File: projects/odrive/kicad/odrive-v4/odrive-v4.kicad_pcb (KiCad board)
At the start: 2 copper layers, 50 x 30 mm, 0 parts

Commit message: Import the v4 netlist onto a 4-layer board, checkpoint before placement
update_pcb_from_schematic (konnect 0.11.0, live IPC, single undo commit)
lands all 378 footprints with 283 nets and zero conflicts. Getting there
took three tries worth of fixes, all kept: the project fp-lib-table now
registers the 18 standard footprint libraries the sheets reference (the
kicad wrapper's KICAD10_FOOTPRINT_DIR is invisible to project resolution,
same story as the symbol libraries); the seven current shunts move to the
real R_Shunt_Vishay_WSK2512_6332Metric_T2.66mm kelvin footprint (the
T1_T2 name the builder invented does not exist); the OV-latch 74LVC1G74
moves to TSSOP-8 (no DCU footprint in this library snapshot - order the
DCT variant); and the SO3 solder jumpers drop the RoundedPad variant
whose custom-shape pads KiCad 10's typed IPC placement path refuses.
Board outline 120x80mm rounded, In1/In2.Cu added file-based after
learning that adding them with pcbnew open gets clobbered by its next
save. Placement not started - components sit stacked at the import
default.
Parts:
- added C1: 100nF 100V X7R, Capacitor_SMD:C_0603_1608Metric, F.Cu at (6.48, 0.73)
- added C10: 470uF/35V | 220uF/63V, Capacitor_THT:CP_Radial_D10.0mm_P5.00mm, F.Cu at (10.4, 119.4)
- added C100: 2.2uF, Capacitor_SMD:C_0603_1608Metric, F.Cu at (6.48, 1695.1)
- added C101: 2.2uF, Capacitor_SMD:C_0603_1608Metric, F.Cu at (6.48, 1701.6)
- added C11: 470uF/35V | 220uF/63V, Capacitor_THT:CP_Radial_D10.0mm_P5.00mm, F.Cu at (10.4, 134.9)
- added C110: 2.2uF 100V X7R, Capacitor_SMD:C_1210_3225Metric, F.Cu at (7.30, 1787.5)
- added C111: 2.2uF 100V X7R, Capacitor_SMD:C_1210_3225Metric, F.Cu at (7.30, 1795.7)
- added C112: 100nF 100V X7R, Capacitor_SMD:C_0603_1608Metric, F.Cu at (6.48, 1803.0)
- added C113: 100nF 25V, Capacitor_SMD:C_0603_1608Metric, F.Cu at (6.48, 1809.5)
- added C114: 22uF 25V X7R, Capacitor_SMD:C_1210_3225Metric, F.Cu at (7.30, 1816.8)
- added C115: 22uF 25V X7R, Capacitor_SMD:C_1210_3225Metric, F.Cu at (7.30, 1825.0)
- added C116: 10uF 25V X7R, Capacitor_SMD:C_0805_2012Metric, F.Cu at (6.70, 1832.6)
- added C117: 100nF 25V, Capacitor_SMD:C_0603_1608Metric, F.Cu at (6.48, 1839.3)
- added C118: 22uF 25V X7R, Capacitor_SMD:C_1210_3225Metric, F.Cu at (7.30, 1846.7)
- added C119: 22uF 25V X7R, Capacitor_SMD:C_1210_3225Metric, F.Cu at (7.30, 1854.8)
- added C120: 68uF 16V polymer, Capacitor_SMD:CP_Elec_6.3x7.7, F.Cu at (9.70, 1865.0)
- added C122: 1uF 16V, Capacitor_SMD:C_0603_1608Metric, F.Cu at (6.48, 1874.3)
- added C123: 1uF 16V, Capacitor_SMD:C_0603_1608Metric, F.Cu at (6.48, 1880.7)
- added C124: 10uF 16V, Capacitor_SMD:C_0805_2012Metric, F.Cu at (6.70, 1887.5)
- added C125: 1uF 16V, Capacitor_SMD:C_0603_1608Metric, F.Cu at (6.48, 1894.2)
- added C126: 100nF, Capacitor_SMD:C_0603_1608Metric, F.Cu at (6.48, 1900.6)
- added C127: 100nF, Capacitor_SMD:C_0603_1608Metric, F.Cu at (6.48, 1907.1)
- added C128: 100nF, Capacitor_SMD:C_0603_1608Metric, F.Cu at (6.48, 1913.5)
- added C129: 100nF, Capacitor_SMD:C_0603_1608Metric, F.Cu at (6.48, 1920.0)
- added C130: 4.7nF, Capacitor_SMD:C_0603_1608Metric, F.Cu at (6.48, 2122.2)
- added C131: 1uF, Capacitor_SMD:C_0603_1608Metric, F.Cu at (6.48, 2128.7)
- added C132: 100nF, Capacitor_SMD:C_0603_1608Metric, F.Cu at (6.48, -2068.7)
- added C133: 100nF, Capacitor_SMD:C_0603_1608Metric, F.Cu at (6.48, -2062.3)
- added C134: 4.7nF, Capacitor_SMD:C_0603_1608Metric, F.Cu at (6.48, -2055.8)
- added C135: 1uF, Capacitor_SMD:C_0603_1608Metric, F.Cu at (6.48, -2049.3)
- added C136: 10uF, Capacitor_SMD:C_0805_2012Metric, F.Cu at (6.70, -2042.6)
- added C140: 1nF, Capacitor_SMD:C_0603_1608Metric, F.Cu at (6.48, -1934.6)
- added C141: 1nF, Capacitor_SMD:C_0603_1608Metric, F.Cu at (6.48, -1928.1)
- added C142: 1nF, Capacitor_SMD:C_0603_1608Metric, F.Cu at (6.48, -1921.7)
- added C143: 1nF, Capacitor_SMD:C_0603_1608Metric, F.Cu at (6.48, -1915.2)
- added C144: 1nF, Capacitor_SMD:C_0603_1608Metric, F.Cu at (6.48, -1908.7)
- added C145: 1nF, Capacitor_SMD:C_0603_1608Metric, F.Cu at (6.48, -1902.3)
- added C146: 10uF, Capacitor_SMD:C_0805_2012Metric, F.Cu at (6.70, -1895.6)
- added C147: 10uF, Capacitor_SMD:C_0805_2012Metric, F.Cu at (6.70, -1888.6)
- added C148: 1nF, Capacitor_SMD:C_0603_1608Metric, F.Cu at (6.48, -1881.9)
- added C149: 1nF, Capacitor_SMD:C_0603_1608Metric, F.Cu at (6.48, -1875.4)
- added C150: 1nF, Capacitor_SMD:C_0603_1608Metric, F.Cu at (6.48, -1869.0)
- added C151: 1nF, Capacitor_SMD:C_0603_1608Metric, F.Cu at (6.48, -1862.5)
- added C152: 1nF, Capacitor_SMD:C_0603_1608Metric, F.Cu at (6.48, -1856.1)
- added C153: 1uF, Capacitor_SMD:C_0603_1608Metric, F.Cu at (6.48, -1849.6)
- added C154: 1uF, Capacitor_SMD:C_0603_1608Metric, F.Cu at (6.48, -1843.1)
- added C155: 100nF, Capacitor_SMD:C_0603_1608Metric, F.Cu at (6.48, -1836.7)
- added C156: 100nF, Capacitor_SMD:C_0603_1608Metric, F.Cu at (6.48, -1830.2)
- added C157: 100nF, Capacitor_SMD:C_0603_1608Metric, F.Cu at (6.48, -1823.8)
- added C158: 100nF, Capacitor_SMD:C_0603_1608Metric, F.Cu at (6.48, -1817.3)
- added C160: 1uF, Capacitor_SMD:C_0603_1608Metric, F.Cu at (6.48, -1534.5)
- added C161: 100nF, Capacitor_SMD:C_0603_1608Metric, F.Cu at (6.48, -1528.0)
- added C162: 100nF, Capacitor_SMD:C_0603_1608Metric, F.Cu at (6.48, -1521.5)
- added C163: 2.2uF 100V X7R, Capacitor_SMD:C_1210_3225Metric, F.Cu at (7.30, -1514.2)
- added C164: 2.2uF 100V X7R, Capacitor_SMD:C_1210_3225Metric, F.Cu at (7.30, -1506.0)
- added C165: 100nF 100V X7R, Capacitor_SMD:C_0603_1608Metric, F.Cu at (6.48, -1498.7)
- added C166: 1nF, Capacitor_SMD:C_0603_1608Metric, F.Cu at (6.48, -1492.2)
- added C167: 100nF, Capacitor_SMD:C_0603_1608Metric, F.Cu at (6.48, -1485.8)
- added C168: 100nF, Capacitor_SMD:C_0603_1608Metric, F.Cu at (6.48, -1479.3)
- added C169: 100nF, Capacitor_SMD:C_0603_1608Metric, F.Cu at (6.48, -1472.8)
- added C170: 100nF, Capacitor_SMD:C_0603_1608Metric, F.Cu at (6.48, -1466.4)
- added C2: 2.2uF 100V X7R, Capacitor_SMD:C_1210_3225Metric, F.Cu at (7.30, 8.06)
- added C20: 2.2uF 100V X7R, Capacitor_SMD:C_1210_3225Metric, F.Cu at (7.30, 262.2)
- added C21: 2.2uF 100V X7R, Capacitor_SMD:C_1210_3225Metric, F.Cu at (7.30, 270.4)
- added C22: 2.2uF 100V X7R, Capacitor_SMD:C_1210_3225Metric, F.Cu at (7.30, 278.6)
- added C23: 2.2uF 100V X7R, Capacitor_SMD:C_1210_3225Metric, F.Cu at (7.30, 286.8)
- added C24: 2.2uF 100V X7R, Capacitor_SMD:C_1210_3225Metric, F.Cu at (7.30, 295.0)
- added C25: 2.2uF 100V X7R, Capacitor_SMD:C_1210_3225Metric, F.Cu at (7.30, 303.2)
- added C26: 100nF 100V X7R, Capacitor_SMD:C_0603_1608Metric, F.Cu at (6.48, 310.5)
- added C27: 100nF 100V X7R, Capacitor_SMD:C_0603_1608Metric, F.Cu at (6.48, 317.0)
- added C28: 100nF 100V X7R, Capacitor_SMD:C_0603_1608Metric, F.Cu at (6.48, 323.4)
- added C29: 47nF 100V X7R, Capacitor_SMD:C_0805_2012Metric, F.Cu at (6.70, 330.1)
- added C3: 1uF 25V, Capacitor_SMD:C_0603_1608Metric, F.Cu at (6.48, 15.4)
- added C30: 1uF, Capacitor_SMD:C_0603_1608Metric, F.Cu at (6.48, 336.9)
- added C31: 1uF, Capacitor_SMD:C_0603_1608Metric, F.Cu at (6.48, 343.3)
- added C32: 1uF 100V X7R, Capacitor_SMD:C_1210_3225Metric, F.Cu at (7.30, 350.6)
- added C33: 100nF, Capacitor_SMD:C_0603_1608Metric, F.Cu at (6.48, 358.0)
- added C34: 100nF, Capacitor_SMD:C_0603_1608Metric, F.Cu at (6.48, 364.4)
- added C35: 1nF, Capacitor_SMD:C_0603_1608Metric, F.Cu at (6.48, 370.9)
- added C36: 1nF, Capacitor_SMD:C_0603_1608Metric, F.Cu at (6.48, 377.4)
- added C37: 1nF, Capacitor_SMD:C_0603_1608Metric, F.Cu at (6.48, 383.8)
- added C4: 470uF/35V | 220uF/63V, Capacitor_THT:CP_Radial_D10.0mm_P5.00mm, F.Cu at (10.4, 26.4)
- added C40: 2.2uF 100V X7R, Capacitor_SMD:C_1210_3225Metric, F.Cu at (7.30, 719.1)
- added C41: 2.2uF 100V X7R, Capacitor_SMD:C_1210_3225Metric, F.Cu at (7.30, 727.3)
- added C42: 2.2uF 100V X7R, Capacitor_SMD:C_1210_3225Metric, F.Cu at (7.30, 735.5)
- added C43: 2.2uF 100V X7R, Capacitor_SMD:C_1210_3225Metric, F.Cu at (7.30, 743.7)
- added C44: 2.2uF 100V X7R, Capacitor_SMD:C_1210_3225Metric, F.Cu at (7.30, 751.9)
- added C45: 2.2uF 100V X7R, Capacitor_SMD:C_1210_3225Metric, F.Cu at (7.30, 760.1)
- added C46: 100nF 100V X7R, Capacitor_SMD:C_0603_1608Metric, F.Cu at (6.48, 767.5)
- added C47: 100nF 100V X7R, Capacitor_SMD:C_0603_1608Metric, F.Cu at (6.48, 773.9)
- added C48: 100nF 100V X7R, Capacitor_SMD:C_0603_1608Metric, F.Cu at (6.48, 780.4)
- added C49: 47nF 100V X7R, Capacitor_SMD:C_0805_2012Metric, F.Cu at (6.70, 787.1)
- added C5: 470uF/35V | 220uF/63V, Capacitor_THT:CP_Radial_D10.0mm_P5.00mm, F.Cu at (10.4, 41.9)
- added C50: 1uF, Capacitor_SMD:C_0603_1608Metric, F.Cu at (6.48, 793.8)
- added C51: 1uF, Capacitor_SMD:C_0603_1608Metric, F.Cu at (6.48, 800.3)
- added C52: 1uF 100V X7R, Capacitor_SMD:C_1210_3225Metric, F.Cu at (7.30, 807.6)
- added C53: 100nF, Capacitor_SMD:C_0603_1608Metric, F.Cu at (6.48, 814.9)
- added C54: 100nF, Capacitor_SMD:C_0603_1608Metric, F.Cu at (6.48, 821.4)
- added C58: 1nF, Capacitor_SMD:C_0603_1608Metric, F.Cu at (6.48, 827.8)
- added C59: 1nF, Capacitor_SMD:C_0603_1608Metric, F.Cu at (6.48, 834.3)
- added C6: 470uF/35V | 220uF/63V, Capacitor_THT:CP_Radial_D10.0mm_P5.00mm, F.Cu at (10.4, 57.4)
- added C60: 1nF, Capacitor_SMD:C_0603_1608Metric, F.Cu at (6.48, 840.8)
- added C61: 100nF, Capacitor_SMD:C_0603_1608Metric, F.Cu at (6.48, 1175.2)
- added C62: 100nF, Capacitor_SMD:C_0603_1608Metric, F.Cu at (6.48, 1181.7)
- added C63: 100nF, Capacitor_SMD:C_0603_1608Metric, F.Cu at (6.48, 1188.1)
- added C64: 100nF, Capacitor_SMD:C_0603_1608Metric, F.Cu at (6.48, 1194.6)
- added C65: 100nF, Capacitor_SMD:C_0603_1608Metric, F.Cu at (6.48, 1201.0)
- added C7: 470uF/35V | 220uF/63V, Capacitor_THT:CP_Radial_D10.0mm_P5.00mm, F.Cu at (10.4, 72.9)
- added C70: 1nF, Capacitor_SMD:C_0603_1608Metric, F.Cu at (6.48, 1207.5)
- added C71: 1nF, Capacitor_SMD:C_0603_1608Metric, F.Cu at (6.48, 1214.0)
- added C72: 1nF, Capacitor_SMD:C_0603_1608Metric, F.Cu at (6.48, 1220.4)
- added C73: 1nF, Capacitor_SMD:C_0603_1608Metric, F.Cu at (6.48, 1226.9)
- added C74: 1nF, Capacitor_SMD:C_0603_1608Metric, F.Cu at (6.48, 1233.3)
- added C75: 1nF, Capacitor_SMD:C_0603_1608Metric, F.Cu at (6.48, 1239.8)
- added C76: 1nF, Capacitor_SMD:C_0603_1608Metric, F.Cu at (6.48, 1246.3)
- added C77: 1nF, Capacitor_SMD:C_0603_1608Metric, F.Cu at (6.48, 1252.7)
- added C78: 47pF, Capacitor_SMD:C_0603_1608Metric, F.Cu at (6.48, 1259.2)
- added C79: 47pF, Capacitor_SMD:C_0603_1608Metric, F.Cu at (6.48, 1265.6)
- added C8: 470uF/35V | 220uF/63V, Capacitor_THT:CP_Radial_D10.0mm_P5.00mm, F.Cu at (10.4, 88.4)
- added C80: 47pF, Capacitor_SMD:C_0603_1608Metric, F.Cu at (6.48, 1272.1)
- added C81: 47pF, Capacitor_SMD:C_0603_1608Metric, F.Cu at (6.48, 1278.6)
- added C82: 47pF, Capacitor_SMD:C_0603_1608Metric, F.Cu at (6.48, 1285.0)
- added C83: 47pF, Capacitor_SMD:C_0603_1608Metric, F.Cu at (6.48, 1291.5)
- added C84: 2.2uF, Capacitor_SMD:C_0603_1608Metric, F.Cu at (6.48, 1297.9)
- added C85: 2.2uF, Capacitor_SMD:C_0603_1608Metric, F.Cu at (6.48, 1304.4)
- added C86: 2.2uF, Capacitor_SMD:C_0603_1608Metric, F.Cu at (6.48, 1310.9)
- added C87: 100nF, Capacitor_SMD:C_0603_1608Metric, F.Cu at (6.48, 1317.3)
- added C88: 100nF, Capacitor_SMD:C_0603_1608Metric, F.Cu at (6.48, 1323.8)
- added C89: 100nF, Capacitor_SMD:C_0603_1608Metric, F.Cu at (6.48, 1330.2)
- added C9: 470uF/35V | 220uF/63V, Capacitor_THT:CP_Radial_D10.0mm_P5.00mm, F.Cu at (10.4, 103.9)
- added C90: 10pF, Capacitor_SMD:C_0603_1608Metric, F.Cu at (6.48, 1630.0)
- added C91: 10pF, Capacitor_SMD:C_0603_1608Metric, F.Cu at (6.48, 1636.5)
- added C92: 100nF, Capacitor_SMD:C_0603_1608Metric, F.Cu at (6.48, 1642.9)
- added C93: 100nF, Capacitor_SMD:C_0603_1608Metric, F.Cu at (6.48, 1649.4)
- added C94: 100nF, Capacitor_SMD:C_0603_1608Metric, F.Cu at (6.48, 1655.8)
- added C95: 100nF, Capacitor_SMD:C_0603_1608Metric, F.Cu at (6.48, 1662.3)
- added C96: 100nF, Capacitor_SMD:C_0603_1608Metric, F.Cu at (6.48, 1668.8)
- added C97: 4.7uF, Capacitor_SMD:C_0805_2012Metric, F.Cu at (6.70, 1675.5)
- added C98: 1uF, Capacitor_SMD:C_0603_1608Metric, F.Cu at (6.48, 1682.2)
- added C99: 100nF, Capacitor_SMD:C_0603_1608Metric, F.Cu at (6.48, 1688.6)
- added D1: STPS41H100CG, Package_TO_SOT_SMD:TO-263-3_TabPin2, F.Cu at (13.3, 150.8)
- added D10: BAT54S, Package_TO_SOT_SMD:SOT-23, F.Cu at (6.93, 1337.7)
- added D11: PESD3V3L1BA, Diode_SMD:D_SOD-323, F.Cu at (6.61, 1346.0)
- added D12: PESD3V3L1BA, Diode_SMD:D_SOD-323, F.Cu at (6.61, 1354.3)
- added D2: SMDJ28A | SMDJ58A, Diode_SMD:D_SMC, F.Cu at (10.1, 164.8)
- added D20: PESD5V0S1BA, Diode_SMD:D_SOD-323, F.Cu at (6.61, 2136.1)
- added D21: BAT54S, Package_TO_SOT_SMD:SOT-23, F.Cu at (6.93, 2144.4)
- added D22: NUP2105L, Package_TO_SOT_SMD:SOT-23, F.Cu at (6.93, -2034.9)
- added D3: BZT52C10, Diode_SMD:D_SOD-123, F.Cu at (7.36, 174.9)
- added F1: MEGA 50A/32V | 60A/70V, odrive_footprints:Fuse_Littelfuse_MEGA_BoltDown, F.Cu at (39.3, 196.0)
- added FB1: BLM21PG221SN1, Inductor_SMD:L_0805_2012Metric, F.Cu at (6.75, 1926.6)
- added FB2: 600R@100MHz, Inductor_SMD:L_0805_2012Metric, F.Cu at (6.75, -2143.0)
- added FB3: DLW32SH101XF2, odrive_footprints:L_CommonMode_Murata_DLW32SH101XF2, F.Cu at (7.38, -2026.7)
- added J1: PC 16/2-ST, odrive_footprints:TerminalBlock_Phoenix_PC-16-2-ST-10.16mm, F.Cu at (15.2, 222.5)
- added J10: ENC_M1_JST-GH, Connector_JST:JST_GH_BM06B-GHS-TBT_1x06-1MP_P1.25mm_Vertical, F.Cu at (11.0, -1796.7)
- added J11: ENC_SPI_JST-GH, Connector_JST:JST_GH_BM06B-GHS-TBT_1x06-1MP_P1.25mm_Vertical, F.Cu at (11.0, -1785.1)
- added J12: GPIO_2x4, Connector_PinHeader_2.54mm:PinHeader_2x04_P2.54mm_Vertical, F.Cu at (8.04, -1771.2)
- added J13: BRAKE_EXT, odrive_footprints:TerminalBlock_Phoenix_PC-16-2-ST-10.16mm, F.Cu at (15.2, -1453.3)
- added J2: M0 A/B/C, odrive_footprints:TerminalBlock_Phoenix_PC-16-3-ST-10.16mm, F.Cu at (21.8, 397.1)
- added J3: M1 A/B/C, odrive_footprints:TerminalBlock_Phoenix_PC-16-3-ST-10.16mm, F.Cu at (21.8, 854.1)
- added J4: FTSH-105-01-L-DV-K, Connector_PinHeader_1.27mm:PinHeader_2x05_P1.27mm_Vertical_SMD, F.Cu at (9.29, 1711.0)
- added J5: FAN 12V 150mA MAX, Connector_PinHeader_2.54mm:PinHeader_1x02_P2.54mm_Vertical, F.Cu at (6.77, 1935.5)
- added J6: USB4105-GF-A, Connector_USB:USB_C_Receptacle_GCT_USB4105-xx-A_16P_TopMnt_Horizontal, F.Cu at (10.3, -2132.7)
- added J7: JST-GH-4 CAN, Connector_JST:JST_GH_BM04B-GHS-TBT_1x04-1MP_P1.25mm_Vertical, F.Cu at (9.73, -2016.9)
- added J8: JST-GH-4 CAN, Connector_JST:JST_GH_BM04B-GHS-TBT_1x04-1MP_P1.25mm_Vertical, F.Cu at (9.73, -2005.3)
- added J9: ENC_M0_JST-GH, Connector_JST:JST_GH_BM06B-GHS-TBT_1x06-1MP_P1.25mm_Vertical, F.Cu at (11.0, -1808.3)
- added JP1: SJ-Closed, Jumper:SolderJumper-2_P1.3mm_Bridged_Pad1.0x1.5mm, F.Cu at (6.65, 1362.2)
- added JP2: SJ-Closed, Jumper:SolderJumper-2_P1.3mm_Bridged_Pad1.0x1.5mm, F.Cu at (6.65, 1369.7)
- added JP3: BOOT0-DFU, Connector_PinHeader_2.54mm:PinHeader_1x02_P2.54mm_Vertical, F.Cu at (6.77, 1722.7)
- added L1: 100uH, Inductor_SMD:L_12x12mm_H8mm, F.Cu at (11.9, 1950.1)
- added L2: 4.7uH, Inductor_SMD:L_Taiyo-Yuden_NR-50xx, F.Cu at (7.80, 1964.5)
- added NT1: NetTie_2, NetTie:NetTie-2_SMD_Pad0.5mm, F.Cu at (5.75, 1972.7)
- added NT2: NetTie_2, NetTie:NetTie-2_SMD_Pad0.5mm, F.Cu at (5.75, 1978.7)
- added Q1: NVMFS5C628NL | BSC027N10NS5, Package_SO:PowerPAK_SO-8_Single, F.Cu at (8.73, 237.5)
- added Q10: NVMFS5C628NL, Package_SO:PowerPAK_SO-8_Single, F.Cu at (8.73, 412.5)
- added Q11: NVMFS5C628NL, Package_SO:PowerPAK_SO-8_Single, F.Cu at (8.73, 423.0)
- added Q12: NVMFS5C628NL, Package_SO:PowerPAK_SO-8_Single, F.Cu at (8.73, 433.5)
- added Q13: NVMFS5C628NL, Package_SO:PowerPAK_SO-8_Single, F.Cu at (8.73, 444.0)
- added Q14: NVMFS5C628NL, Package_SO:PowerPAK_SO-8_Single, F.Cu at (8.73, 454.5)
- added Q15: NVMFS5C628NL, Package_SO:PowerPAK_SO-8_Single, F.Cu at (8.73, 465.0)
- added Q16: NVMFS5C628NL, Package_SO:PowerPAK_SO-8_Single, F.Cu at (8.73, 475.5)
- added Q17: NVMFS5C628NL, Package_SO:PowerPAK_SO-8_Single, F.Cu at (8.73, 486.0)
- added Q18: NVMFS5C628NL, Package_SO:PowerPAK_SO-8_Single, F.Cu at (8.73, 496.5)
- added Q19: NVMFS5C628NL, Package_SO:PowerPAK_SO-8_Single, F.Cu at (8.73, 507.0)
- added Q20: NVMFS5C628NL, Package_SO:PowerPAK_SO-8_Single, F.Cu at (8.73, 517.5)
- added Q21: NVMFS5C628NL, Package_SO:PowerPAK_SO-8_Single, F.Cu at (8.73, 528.0)
- added Q30: NVMFS5C628NL, Package_SO:PowerPAK_SO-8_Single, F.Cu at (8.73, 869.4)
- added Q31: NVMFS5C628NL, Package_SO:PowerPAK_SO-8_Single, F.Cu at (8.73, 879.9)
- added Q32: NVMFS5C628NL, Package_SO:PowerPAK_SO-8_Single, F.Cu at (8.73, 890.4)
- added Q33: NVMFS5C628NL, Package_SO:PowerPAK_SO-8_Single, F.Cu at (8.73, 900.9)
- added Q34: NVMFS5C628NL, Package_SO:PowerPAK_SO-8_Single, F.Cu at (8.73, 911.4)
- added Q35: NVMFS5C628NL, Package_SO:PowerPAK_SO-8_Single, F.Cu at (8.73, 921.9)
- added Q36: NVMFS5C628NL, Package_SO:PowerPAK_SO-8_Single, F.Cu at (8.73, 932.4)
- added Q37: NVMFS5C628NL, Package_SO:PowerPAK_SO-8_Single, F.Cu at (8.73, 942.9)
- added Q38: NVMFS5C628NL, Package_SO:PowerPAK_SO-8_Single, F.Cu at (8.73, 953.4)
- added Q39: NVMFS5C628NL, Package_SO:PowerPAK_SO-8_Single, F.Cu at (8.73, 963.9)
- added Q40: NVMFS5C628NL, Package_SO:PowerPAK_SO-8_Single, F.Cu at (8.73, 974.4)
- added Q41: NVMFS5C628NL, Package_SO:PowerPAK_SO-8_Single, F.Cu at (8.73, 984.9)
- added Q50: NVMFS5C628NL/BSC027N10NS5, Package_SO:PowerPAK_SO-8_Single, F.Cu at (8.73, -1438.3)
- added Q51: NVMFS5C628NL/BSC027N10NS5, Package_SO:PowerPAK_SO-8_Single, F.Cu at (8.73, -1427.8)
- added R1: 100R 2W, Resistor_SMD:R_2512_6332Metric, F.Cu at (8.83, 247.2)
- added R10: 2.2R, Resistor_SMD:R_0603_1608Metric, F.Cu at (6.48, 536.5)
- added R100: 10k, Resistor_SMD:R_0603_1608Metric, F.Cu at (6.48, 1731.5)
- added R101: 47k, Resistor_SMD:R_0603_1608Metric, F.Cu at (6.48, 1737.9)
- added R102: 10k, Resistor_SMD:R_0603_1608Metric, F.Cu at (6.48, 1744.4)
- added R11: 2.2R, Resistor_SMD:R_0603_1608Metric, F.Cu at (6.48, 542.9)
- added R110: 90.9k, Resistor_SMD:R_0603_1608Metric, F.Cu at (6.48, 1985.0)
- added R111: 10k, Resistor_SMD:R_0603_1608Metric, F.Cu at (6.48, 1991.4)
- added R112: 73.2k, Resistor_SMD:R_0603_1608Metric, F.Cu at (6.48, 1997.9)
- added R113: 10k, Resistor_SMD:R_0603_1608Metric, F.Cu at (6.48, 2004.3)
- added R115: 10k, Resistor_SMD:R_0603_1608Metric, F.Cu at (6.48, 2010.8)
- added R116: 26.1k, Resistor_SMD:R_0603_1608Metric, F.Cu at (6.48, 2017.2)
- added R117: 10k, Resistor_SMD:R_0603_1608Metric, F.Cu at (6.48, 2023.7)
- added R118: 301k, Resistor_SMD:R_0603_1608Metric, F.Cu at (6.48, 2030.2)
- added R119: 10k, Resistor_SMD:R_0603_1608Metric, F.Cu at (6.48, 2036.6)
- added R12: 2.2R, Resistor_SMD:R_0603_1608Metric, F.Cu at (6.48, 549.4)
- added R120: 5.1k, Resistor_SMD:R_0603_1608Metric, F.Cu at (6.48, -2122.5)
- added R121: 5.1k, Resistor_SMD:R_0603_1608Metric, F.Cu at (6.48, -2116.0)
- added R122: 22R, Resistor_SMD:R_0603_1608Metric, F.Cu at (6.48, -2109.6)
- added R123: 22R, Resistor_SMD:R_0603_1608Metric, F.Cu at (6.48, -2103.1)
- added R124: 1M, Resistor_SMD:R_0603_1608Metric, F.Cu at (6.48, -2096.6)
- added R125: 47k, Resistor_SMD:R_0603_1608Metric, F.Cu at (6.48, -2090.2)
- added R126: 10k, Resistor_SMD:R_0603_1608Metric, F.Cu at (6.48, -2083.7)
- added R127: 60R, Resistor_SMD:R_0603_1608Metric, F.Cu at (6.48, -1996.3)
- added R128: 60R, Resistor_SMD:R_0603_1608Metric, F.Cu at (6.48, -1989.8)
- added R129: 56k, Resistor_SMD:R_0603_1608Metric, F.Cu at (6.48, -1983.3)
- added R13: 2.2R, Resistor_SMD:R_0603_1608Metric, F.Cu at (6.48, 555.9)
- added R130: 0R, Resistor_SMD:R_0603_1608Metric, F.Cu at (6.48, -1976.9)
- added R131: 0R, Resistor_SMD:R_0603_1608Metric, F.Cu at (6.48, -1970.4)
- added R14: 2.2R, Resistor_SMD:R_0603_1608Metric, F.Cu at (6.48, 562.3)
- added R15: 2.2R, Resistor_SMD:R_0603_1608Metric, F.Cu at (6.48, 568.8)
- added R16: 2.2R, Resistor_SMD:R_0603_1608Metric, F.Cu at (6.48, 575.2)
- added R160: 50R/150R, Resistor_SMD:R_2512_6332Metric, F.Cu at (8.83, -1418.1)
- added R161: 2.2R, Resistor_SMD:R_0603_1608Metric, F.Cu at (6.48, -1410.5)
- added R162: 2.2R, Resistor_SMD:R_0603_1608Metric, F.Cu at (6.48, -1404.0)
- added R163: 47k, Resistor_SMD:R_0603_1608Metric, F.Cu at (6.48, -1397.5)
- added R164: 2mR, Resistor_SMD:R_Shunt_Vishay_WSK2512_6332Metric_T2.66mm, F.Cu at (9.38, -1389.9)
- added R165: 3.3k, Resistor_SMD:R_0603_1608Metric, F.Cu at (6.48, -1382.3)
- added R166: 10k, Resistor_SMD:R_0603_1608Metric, F.Cu at (6.48, -1375.8)
- added R167: 10k, Resistor_SMD:R_0603_1608Metric, F.Cu at (6.48, -1369.4)
- added R168: 1R, Resistor_SMD:R_0603_1608Metric, F.Cu at (6.48, -1362.9)
- added R17: 2.2R, Resistor_SMD:R_0603_1608Metric, F.Cu at (6.48, 581.7)
- added R170: 2.2R 1W, Resistor_SMD:R_2512_6332Metric, F.Cu at (8.83, 2044.3)
- added R18: 2.2R, Resistor_SMD:R_0603_1608Metric, F.Cu at (6.48, 588.2)
- added R180: 3.3k, Resistor_SMD:R_0603_1608Metric, F.Cu at (6.48, -1759.9)
- added R181: 3.3k, Resistor_SMD:R_0603_1608Metric, F.Cu at (6.48, -1753.4)
- added R182: 3.3k, Resistor_SMD:R_0603_1608Metric, F.Cu at (6.48, -1747.0)
- added R183: 3.3k, Resistor_SMD:R_0603_1608Metric, F.Cu at (6.48, -1740.5)
- added R184: 3.3k, Resistor_SMD:R_0603_1608Metric, F.Cu at (6.48, -1734.0)
- added R185: 3.3k, Resistor_SMD:R_0603_1608Metric, F.Cu at (6.48, -1727.6)
- added R186: 100R, Resistor_SMD:R_0603_1608Metric, F.Cu at (6.48, -1721.1)
- added R187: 100R, Resistor_SMD:R_0603_1608Metric, F.Cu at (6.48, -1714.7)
- added R188: 100R, Resistor_SMD:R_0603_1608Metric, F.Cu at (6.48, -1708.2)
- added R189: 100R, Resistor_SMD:R_0603_1608Metric, F.Cu at (6.48, -1701.7)
- added R19: 2.2R, Resistor_SMD:R_0603_1608Metric, F.Cu at (6.48, 594.6)
- added R190: 100R, Resistor_SMD:R_0603_1608Metric, F.Cu at (6.48, -1695.3)
- added R191: 100R, Resistor_SMD:R_0603_1608Metric, F.Cu at (6.48, -1688.8)
- added R192: 56k, Resistor_SMD:R_0603_1608Metric, F.Cu at (6.48, -1682.4)
- added R193: 56k, Resistor_SMD:R_0603_1608Metric, F.Cu at (6.48, -1675.9)
- added R194: 470R, Resistor_SMD:R_0603_1608Metric, F.Cu at (6.48, -1669.4)
- added R195: 470R, Resistor_SMD:R_0603_1608Metric, F.Cu at (6.48, -1663.0)
- added R196: 470R, Resistor_SMD:R_0603_1608Metric, F.Cu at (6.48, -1656.5)
- added R197: 100R, Resistor_SMD:R_0603_1608Metric, F.Cu at (6.48, -1650.1)
- added R198: 100R, Resistor_SMD:R_0603_1608Metric, F.Cu at (6.48, -1643.6)
- added R199: 100R, Resistor_SMD:R_0603_1608Metric, F.Cu at (6.48, -1637.1)
- added R2: 1M, Resistor_SMD:R_0603_1608Metric, F.Cu at (6.48, 254.9)
- added R20: 2.2R, Resistor_SMD:R_0603_1608Metric, F.Cu at (6.48, 601.1)
- added R200: 100R, Resistor_SMD:R_0603_1608Metric, F.Cu at (6.48, -1630.7)
- added R201: 100R, Resistor_SMD:R_0603_1608Metric, F.Cu at (6.48, -1624.2)
- added R21: 2.2R, Resistor_SMD:R_0603_1608Metric, F.Cu at (6.48, 607.5)
- added R22: 1mR, Resistor_SMD:R_Shunt_Vishay_WSK2512_6332Metric_T2.66mm, F.Cu at (9.38, 615.2)
- added R23: 1mR, Resistor_SMD:R_Shunt_Vishay_WSK2512_6332Metric_T2.66mm, F.Cu at (9.38, 624.0)
- added R24: 1mR, Resistor_SMD:R_Shunt_Vishay_WSK2512_6332Metric_T2.66mm, F.Cu at (9.38, 632.8)
- added R25: 10k, Resistor_SMD:R_0603_1608Metric, F.Cu at (6.48, 640.4)
- added R26: 10k, Resistor_SMD:R_0603_1608Metric, F.Cu at (6.48, 646.9)
- added R27: 10k, Resistor_SMD:R_0603_1608Metric, F.Cu at (6.48, 653.3)
- added R28: 10k, Resistor_SMD:R_0603_1608Metric, F.Cu at (6.48, 659.8)
- added R29: 10k, Resistor_SMD:R_0603_1608Metric, F.Cu at (6.48, 666.2)
- added R30: 10k, Resistor_SMD:R_0603_1608Metric, F.Cu at (6.48, 672.7)
- added R31: 1R, Resistor_SMD:R_0603_1608Metric, F.Cu at (6.48, 679.2)
- added R32: 1R, Resistor_SMD:R_0603_1608Metric, F.Cu at (6.48, 685.6)
- added R33: 1R, Resistor_SMD:R_0603_1608Metric, F.Cu at (6.48, 692.1)
- added R37: 10k, Resistor_SMD:R_0603_1608Metric, F.Cu at (6.48, 698.5)
- added R40: 2.2R, Resistor_SMD:R_0603_1608Metric, F.Cu at (6.48, 993.4)
- added R41: 2.2R, Resistor_SMD:R_0603_1608Metric, F.Cu at (6.48, 999.9)
- added R42: 2.2R, Resistor_SMD:R_0603_1608Metric, F.Cu at (6.48, 1006.3)
- added R43: 2.2R, Resistor_SMD:R_0603_1608Metric, F.Cu at (6.48, 1012.8)
- added R44: 2.2R, Resistor_SMD:R_0603_1608Metric, F.Cu at (6.48, 1019.3)
- added R45: 2.2R, Resistor_SMD:R_0603_1608Metric, F.Cu at (6.48, 1025.7)
- added R46: 2.2R, Resistor_SMD:R_0603_1608Metric, F.Cu at (6.48, 1032.2)
- added R47: 2.2R, Resistor_SMD:R_0603_1608Metric, F.Cu at (6.48, 1038.6)
- added R48: 2.2R, Resistor_SMD:R_0603_1608Metric, F.Cu at (6.48, 1045.1)
- added R49: 2.2R, Resistor_SMD:R_0603_1608Metric, F.Cu at (6.48, 1051.6)
- added R50: 2.2R, Resistor_SMD:R_0603_1608Metric, F.Cu at (6.48, 1058.0)
- added R51: 2.2R, Resistor_SMD:R_0603_1608Metric, F.Cu at (6.48, 1064.5)
- added R52: 1mR, Resistor_SMD:R_Shunt_Vishay_WSK2512_6332Metric_T2.66mm, F.Cu at (9.38, 1072.1)
- added R53: 1mR, Resistor_SMD:R_Shunt_Vishay_WSK2512_6332Metric_T2.66mm, F.Cu at (9.38, 1080.9)
- added R54: 1mR, Resistor_SMD:R_Shunt_Vishay_WSK2512_6332Metric_T2.66mm, F.Cu at (9.38, 1089.7)
- added R55: 10k, Resistor_SMD:R_0603_1608Metric, F.Cu at (6.48, 1097.3)
- added R56: 10k, Resistor_SMD:R_0603_1608Metric, F.Cu at (6.48, 1103.8)
- added R57: 10k, Resistor_SMD:R_0603_1608Metric, F.Cu at (6.48, 1110.3)
- added R58: 10k, Resistor_SMD:R_0603_1608Metric, F.Cu at (6.48, 1116.7)
- added R59: 10k, Resistor_SMD:R_0603_1608Metric, F.Cu at (6.48, 1123.2)
- added R60: 10k, Resistor_SMD:R_0603_1608Metric, F.Cu at (6.48, 1129.6)
- added R61: 10k, Resistor_SMD:R_0603_1608Metric, F.Cu at (6.48, 1136.1)
- added R64: 1R, Resistor_SMD:R_0603_1608Metric, F.Cu at (6.48, 1142.6)
- added R65: 1R, Resistor_SMD:R_0603_1608Metric, F.Cu at (6.48, 1149.0)
- added R66: 1R, Resistor_SMD:R_0603_1608Metric, F.Cu at (6.48, 1155.5)
- added R70: 10k | 18k, Resistor_SMD:R_0603_1608Metric, F.Cu at (6.48, 1376.7)
- added R71: 1k, Resistor_SMD:R_0603_1608Metric, F.Cu at (6.48, 1383.2)
- added R72: 100R, Resistor_SMD:R_0603_1608Metric, F.Cu at (6.48, 1389.6)
- added R73: 100R, Resistor_SMD:R_0603_1608Metric, F.Cu at (6.48, 1396.1)
- added R74: 100R, Resistor_SMD:R_0603_1608Metric, F.Cu at (6.48, 1402.5)
- added R75: 100R, Resistor_SMD:R_0603_1608Metric, F.Cu at (6.48, 1409.0)
- added R76: 100R, Resistor_SMD:R_0603_1608Metric, F.Cu at (6.48, 1415.5)
- added R77: 100R, Resistor_SMD:R_0603_1608Metric, F.Cu at (6.48, 1421.9)
- added R78: 100R, Resistor_SMD:R_0603_1608Metric, F.Cu at (6.48, 1428.4)
- added R79: 100R, Resistor_SMD:R_0603_1608Metric, F.Cu at (6.48, 1434.8)
- added R80: 100R, Resistor_SMD:R_0603_1608Metric, F.Cu at (6.48, 1441.3)
- added R81: 100R, Resistor_SMD:R_0603_1608Metric, F.Cu at (6.48, 1447.8)
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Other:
- board size 50 x 30 mm -> 120 x 80 mm
- copper layers 2 -> 4

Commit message: Replace konnect's placement grid with a shelf packer; fill the v4 board
The clustering fix alone still overflowed vertically, because the grid packer
padded every cell in a cluster to that cluster's biggest part — a mixed-size
group (an electrolytic beside a row of 0402s) wasted ~20x its real area. This
replaces the padded per-cluster grid with a shelf packer: each part is placed
at its own courtyard size, clusters kept contiguous so a signal group lands
together, shelves wrapping at the board's right edge. Tightly-packed, the 378
parts need ~14,000 mm2, so the board outline grows from an arbitrary 120x80 to
160x110 mm (the design doc leaves form factor free). Verified end to end with
the patched binary file-based: all 378 footprints land inside the outline —
a real first placement where before nothing reached the board at all.

Still a starting point, not a final layout: parts are packed by cluster order,
not yet grouped into the power-left / logic-right floor plan of design doc 6,
and tight courtyards will need spacing during refinement. But the board is
populated and on-board, which is the thing that was impossible before.
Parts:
- moved FB2 2246.4 mm to (96.5, 101.6)
- moved R120 2232.7 mm to (106.7, 108.0)
- moved R121 2226.4 mm to (110.5, 108.0)
- moved R122 2220.2 mm to (115.6, 108.0)
- moved R123 2213.9 mm to (119.4, 108.0)
- moved R124 2207.7 mm to (124.5, 108.0)
- moved R125 2201.5 mm to (128.3, 108.0)
- moved J6 2196.4 mm to (195.6, 55.9)
- moved R126 2195.3 mm to (133.3, 108.0)
- moved C132 2195.3 mm to (66.0, 125.7)
- moved C133 2188.9 mm to (71.1, 125.7)
- moved U33 2178.3 mm to (143.5, 97.8)
- moved C135 2176.1 mm to (74.9, 125.7)
- moved C134 2161.4 mm to (137.2, 101.6)
- moved C136 2144.9 mm to (58.4, 101.6)
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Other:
- board size 120 x 80 mm -> 160 x 110 mm

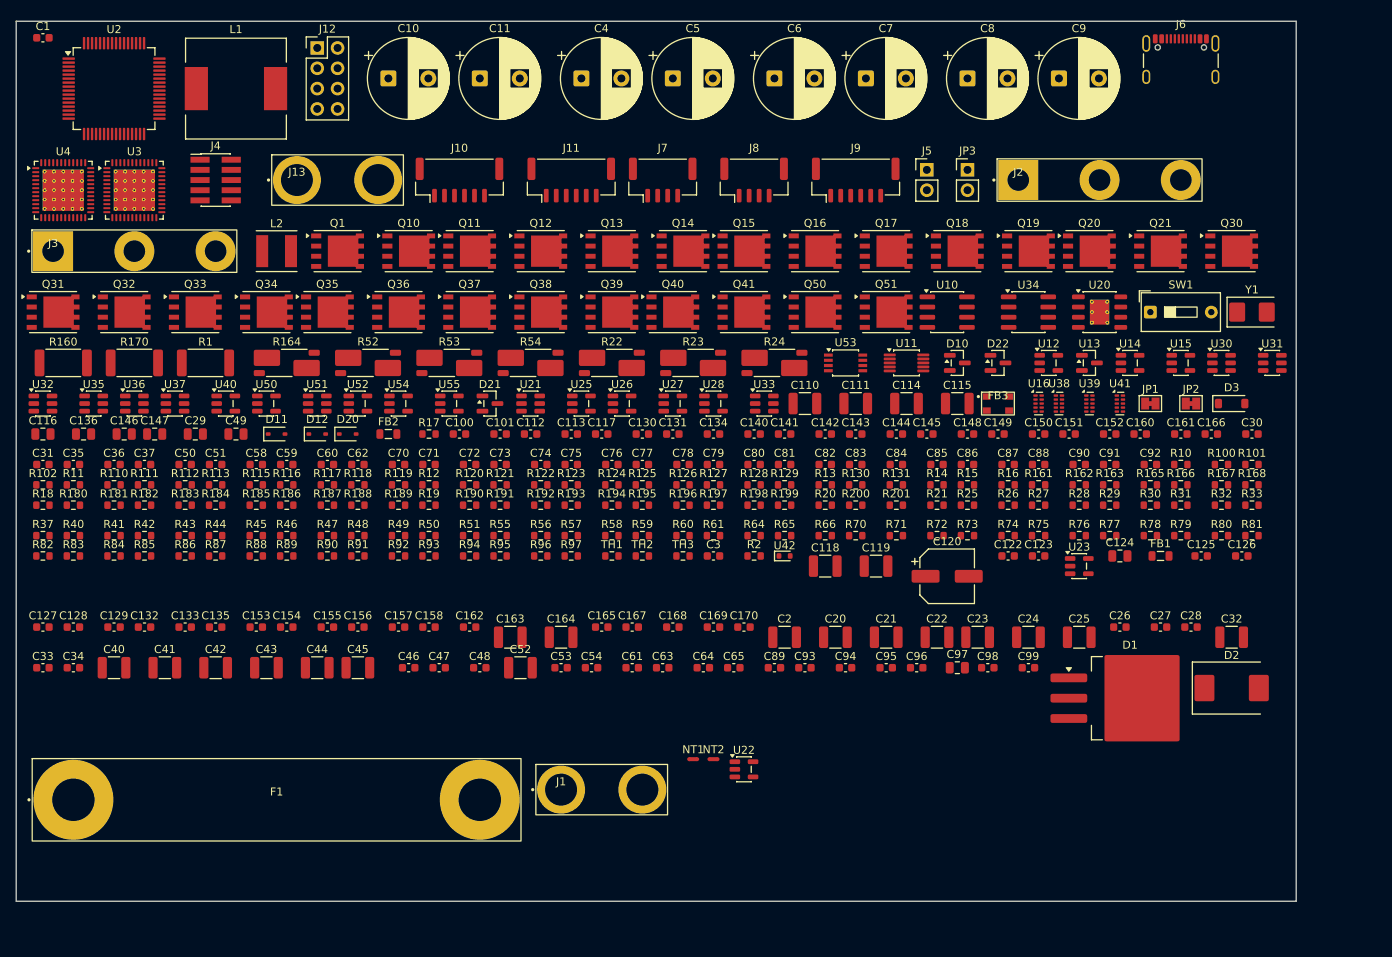
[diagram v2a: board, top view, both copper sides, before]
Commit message: Optimize the single-sided placement with the ODrive floor plan
Replaces the generic shelf-pack with a reference-guided region layout, now
that the imported ODrive PcbDoc gives the proven structure: the two motor
cells top-left and top-right, DC input + fuse + electrolytics + MCU across
the top-centre, and all logic (sensing, rails, brake, CAN, USB, encoders)
in the lower bands with connectors along the bottom edge. Single-sided at
170x115mm - more spread and readable than the cramped double-sided variant
(64 courtyard overlaps vs 103, none outside the outline), because one side
has twice the room per region. Structure is done; the remaining courtyard
overlaps (pad-extent packing underestimates true courtyards) are a manual
spread-apart pass. The double-sided variant stays in odrive-v4-2side.kicad_pcb.
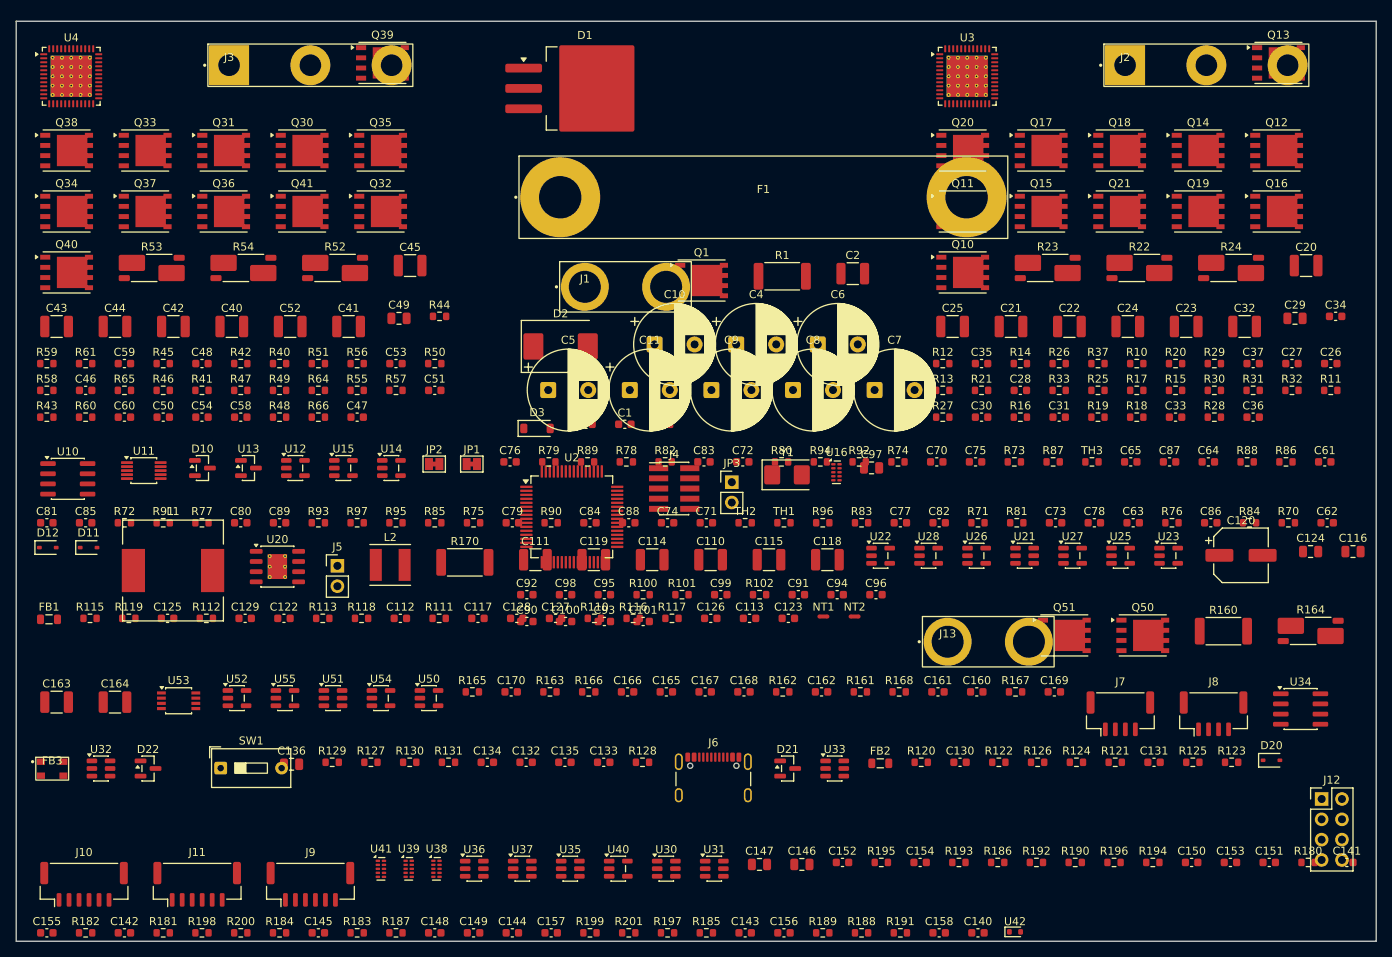
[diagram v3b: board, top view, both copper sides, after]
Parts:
- moved C116 164.4 mm to (217.1, 116.3)
- moved C34 163.8 mm to (214.9, 86.9)
- moved R180 160.7 mm to (211.5, 155.2)
- moved R11 157.6 mm to (214.3, 96.1)
- moved J12 156.8 mm to (213.2, 147.2)
- moved R160 148.8 mm to (200.9, 126.2)
- moved C33 145.0 mm to (194.9, 99.5)
- moved C36 142.5 mm to (204.6, 99.5)
- moved R84 142.0 mm to (204.2, 112.7)
- moved FB1 139.2 mm to (54.1, 124.8)
- moved C37 139.2 mm to (204.6, 92.8)
- moved C29 138.2 mm to (209.8, 87.1)
- moved R86 138.1 mm to (208.7, 105.1)
- moved R18 137.2 mm to (190.1, 99.5)
- moved R37 133.6 mm to (185.2, 92.8)
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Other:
- board size 160 x 110 mm -> 170 x 115 mm

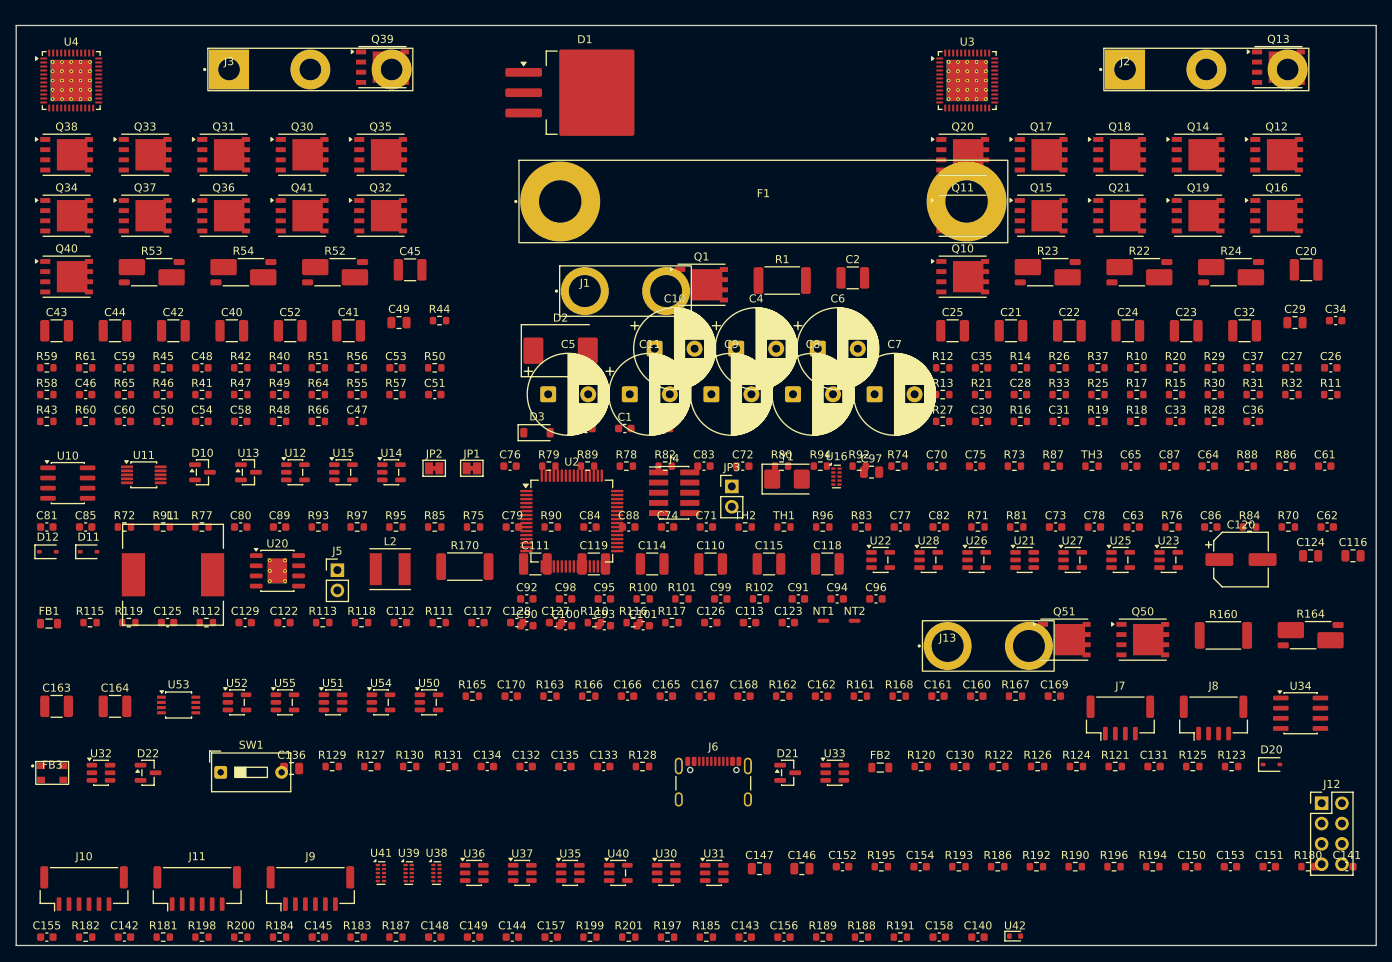
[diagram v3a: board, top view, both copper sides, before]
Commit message: Clear all placement overlaps: single-sided v4 now legal (verdict pass)
Wrote a courtyard collision-resolver (parse each footprint's F.CrtYd bbox in
board coords, iteratively push overlapping pairs apart along the shallower
penetration axis, clamp inside the outline, snap to 0.5mm) and drove it in a
resolve->apply->score loop against konnect's score_placement oracle. Took the
ODrive-structured single-sided placement from 64 courtyard overlaps to zero:
verdict pass, score 40. Placement-only (set_component_placements), netlist
untouched. Remaining score deductions are connector-not-at-edge and
decoupling-distance - quality, not legality - and are the next refinement.
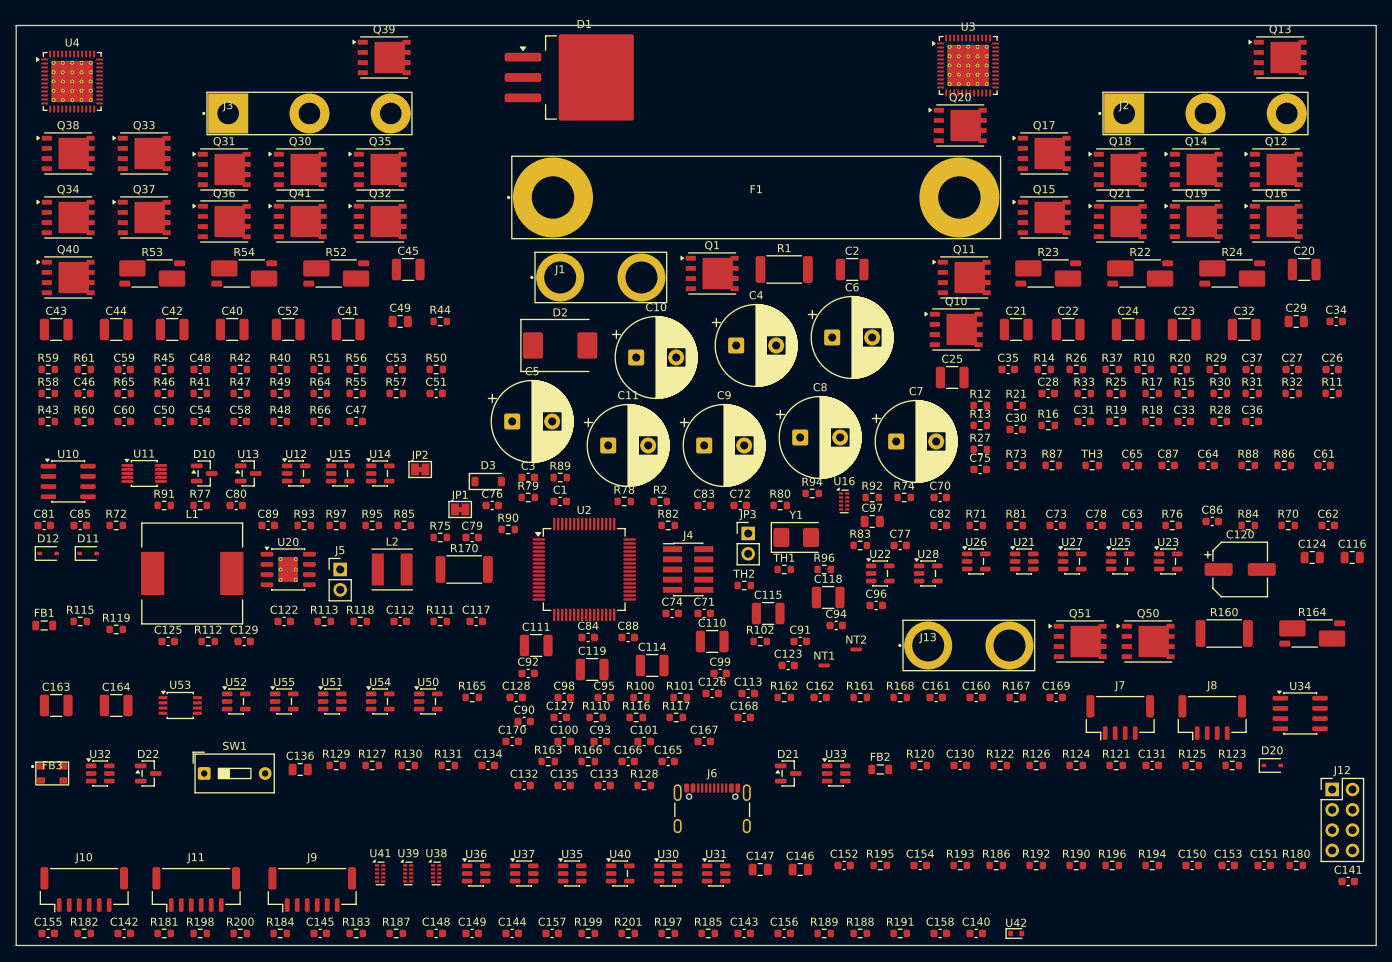
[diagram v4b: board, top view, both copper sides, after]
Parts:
- moved C93 14.5 mm to (123.0, 139.5)
- moved C100 14.5 mm to (118.5, 139.5)
- moved C101 14.5 mm to (128.5, 139.5)
- moved C84 13.8 mm to (121.5, 126.5)
- moved C88 13.8 mm to (126.5, 126.5)
- moved C119 13.2 mm to (122.0, 130.5)
- moved C114 12.7 mm to (129.5, 130.0)
- moved R100 12.3 mm to (128.0, 134.0)
- moved R101 12.3 mm to (133.0, 134.0)
- moved C98 12.3 mm to (118.5, 134.0)
- moved C95 12.3 mm to (123.5, 134.0)
- moved C1 12.2 mm to (118.0, 109.5)
- moved C90 12.0 mm to (113.5, 137.0)
- moved C127 11.9 mm to (118.0, 136.5)
- moved R117 11.9 mm to (132.5, 136.5)
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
